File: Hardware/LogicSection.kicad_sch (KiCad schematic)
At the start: 10 parts, among them J1 Conn_01x03, J2 Conn_01x03, J3 Conn_01x02

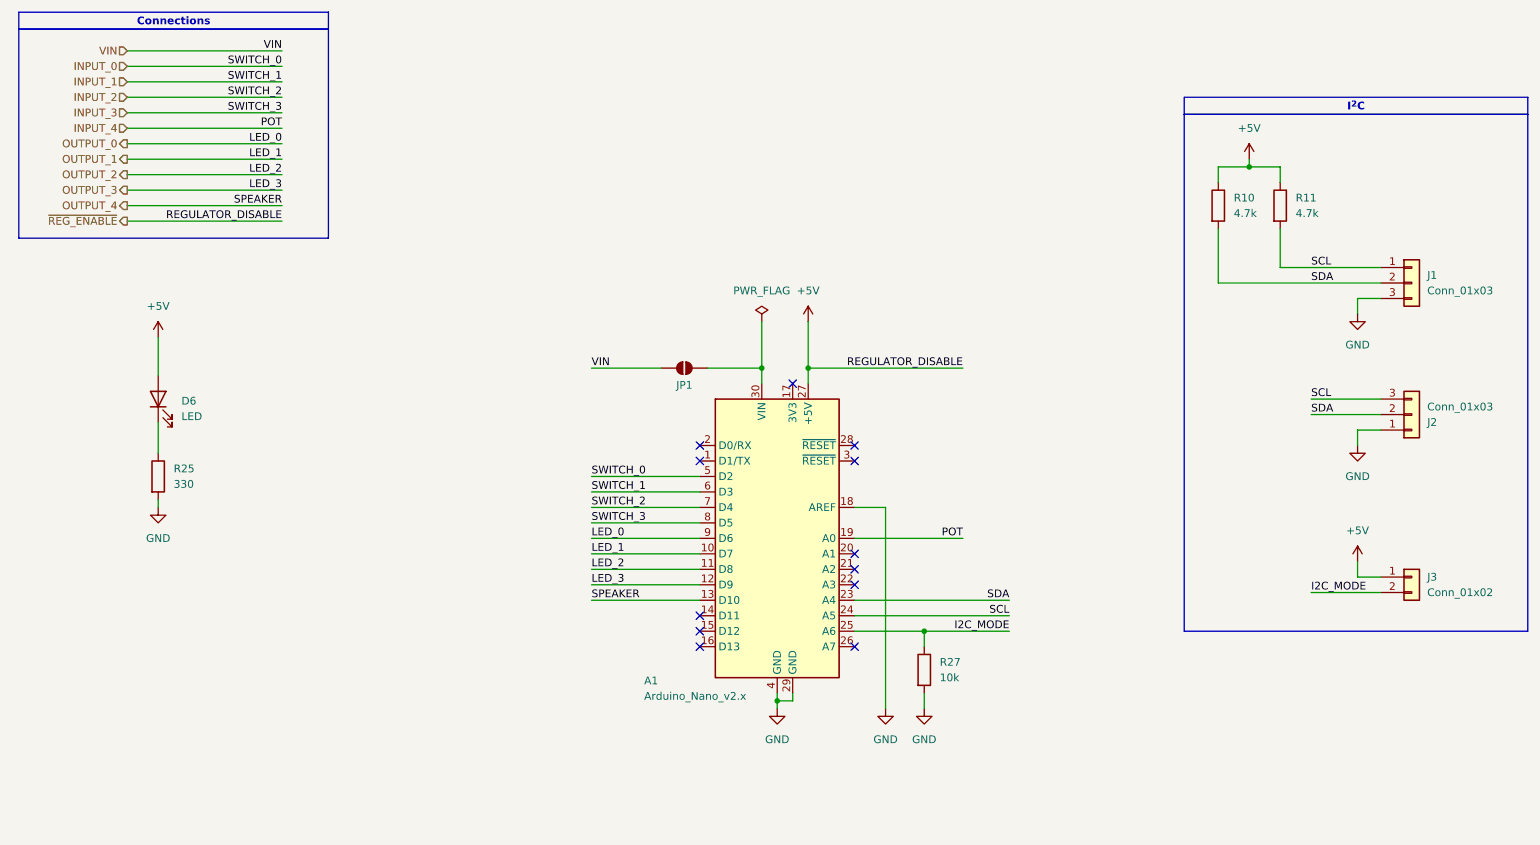
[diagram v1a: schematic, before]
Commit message: Updated KiCAD project.
- Added grouping in schematics.
- Removed unnecessary net names in "LogicSection.kicad_sch".
- Added 330R between +5V and nREG_ENABLE.
- Changed path for 3D models.
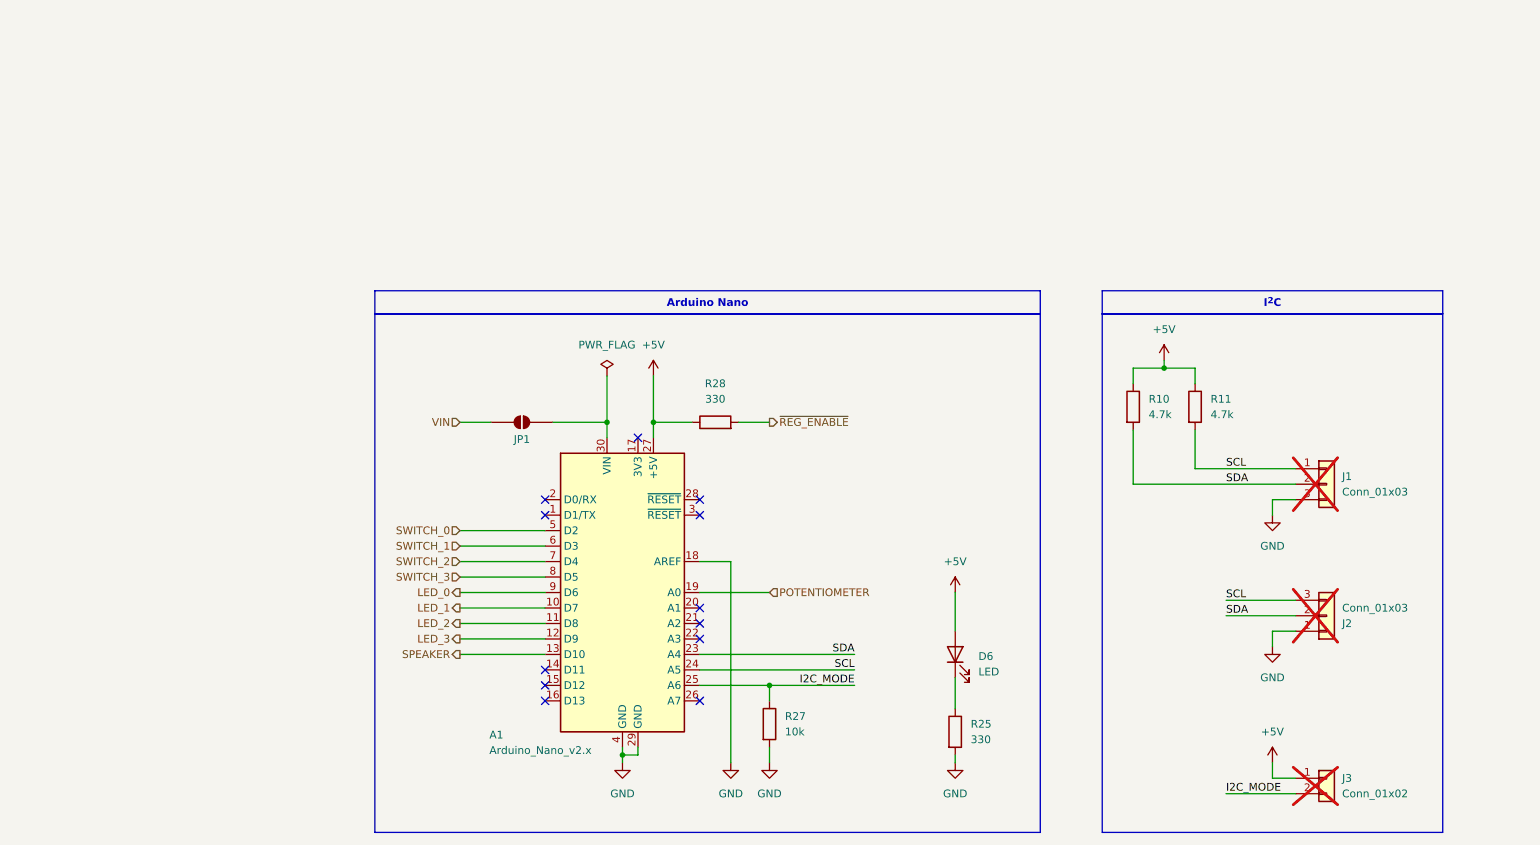
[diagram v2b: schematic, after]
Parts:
- added R28: 330, Resistor_SMD:R_0805_2012Metric, symbol Device:R
- J1, J2, J3: now not fitted
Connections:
- net +5V: now also R28.1
- net INPUT_0 renamed SWITCH_0
- net INPUT_1 renamed SWITCH_1
- net INPUT_2 renamed SWITCH_2
- net INPUT_3 renamed SWITCH_3
- net INPUT_4 renamed POTENTIOMETER
- net OUTPUT_0 renamed LED_0
- net OUTPUT_1 renamed LED_1
- net OUTPUT_2 renamed LED_2
- net OUTPUT_3 renamed LED_3
- net OUTPUT_4 renamed SPEAKER
- new net ~{REG_ENABLE}: R28.2
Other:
- moved on the sheet: A1, D6, JP1, R10, R11, R25, R27
